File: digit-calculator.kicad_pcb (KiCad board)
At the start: 2 copper layers, 38.5 x 45 mm, 7 parts, among them J1 3V3, J2 - +, SW1 Switch, U1 XIAO this side

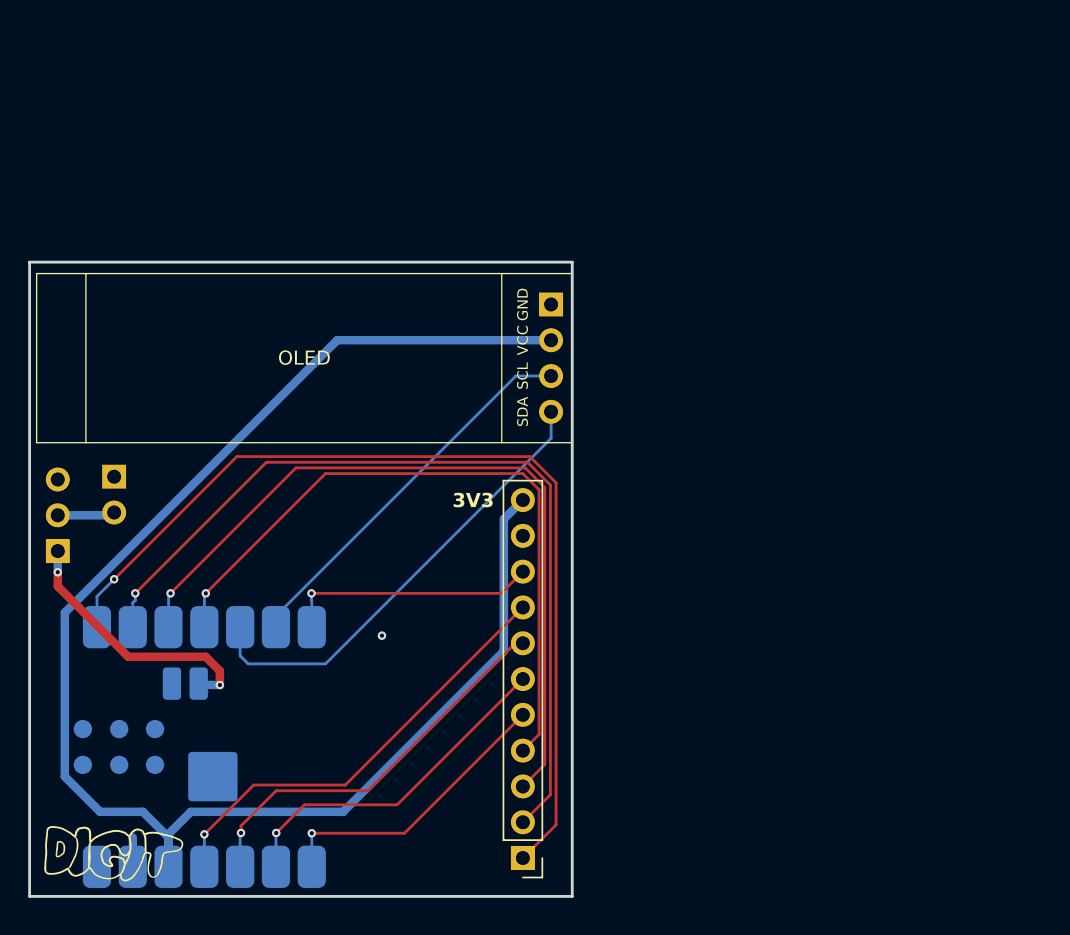
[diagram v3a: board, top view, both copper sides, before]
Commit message: switch to a bigger OLED, add more silkscreen, reroute everything, resize the board
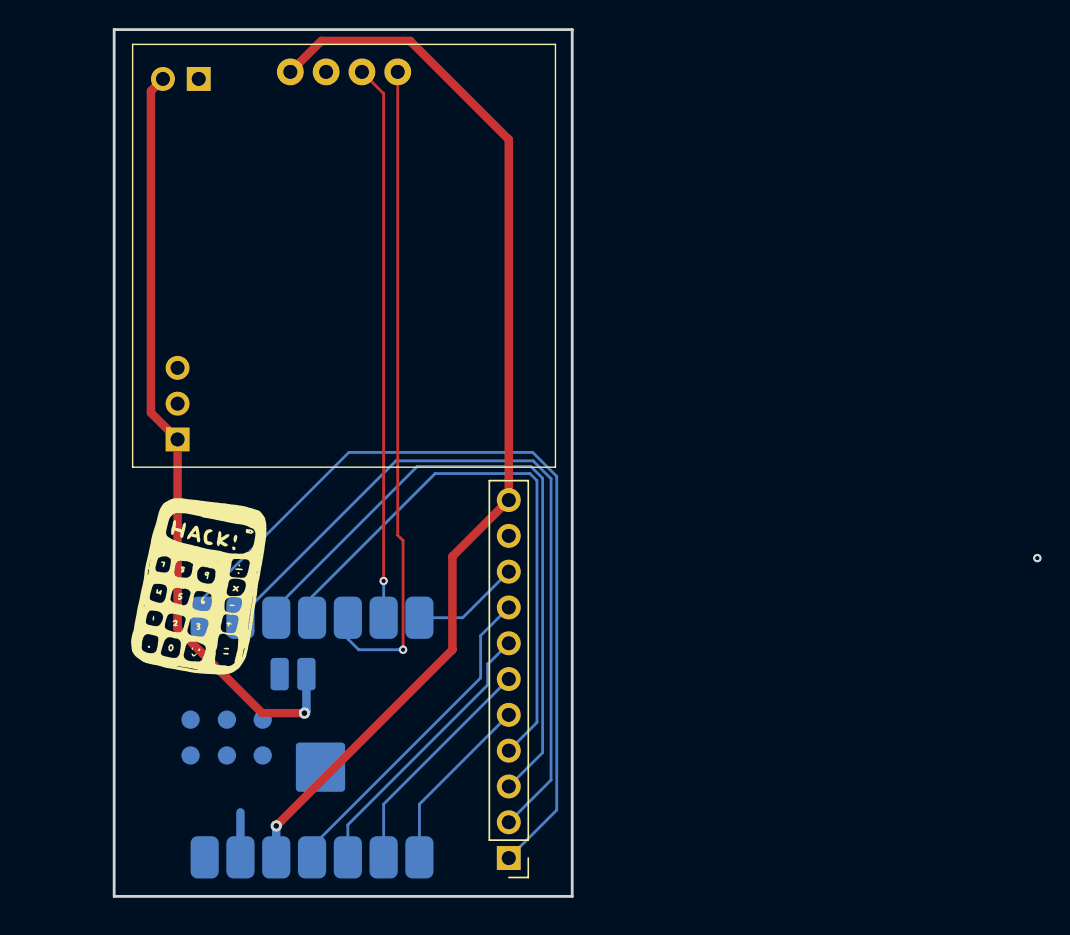
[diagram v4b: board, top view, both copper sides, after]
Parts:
- added logo: LOGO, LOGO, B.Cu at (171.0, 49.0)
- Brd1: footprint Display:SSD1306-0.91-OLED-4pin-128x32 -> Display:SSD1306-OLED
- J1: value 3V3 -> Trackball
- U1: value XIAO this side -> xiao this side down
- moved J2 28.9 mm to (156.5, 36.5), turned to 90 degrees
- moved Brd1 26.1 mm to (166.8, 36.0)
- moved G*** 19.9 mm to (156.5, 72.5)
- moved G*** 16.3 mm to (172.1, 38.7)
- moved SW1 11.6 mm to (155.0, 62.1)
- moved U1 7.67 mm to (164.5, 83.2)
- moved J1 1.00 mm to (178.5, 91.8)
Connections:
- Brd1 pad 1: GND -> +3V3
- Brd1 pad 2: +3V3 -> /SCL
- SW1 pad 2: +BATT -> Net-(SW1-B)
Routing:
- net +3V3: track 108.1 -> 77.1 mm, vias 0 -> 1
- net +BATT: track 24.0 -> 54.4 mm, vias 2 -> 1
- net /SDA: track 32.8 -> 46.9 mm, vias 0 -> 1
- net /SCL: track 27.4 -> 39.4 mm, vias 0 -> 1
- net /BTN: track 18.0 -> 7.69 mm, vias 1 -> 0
- net /J_RIGHT: track 32.9 -> 23.5 mm, vias 1 -> 0
- net /J_LEFT: track 28.3 -> 19.9 mm, vias 1 -> 0
- net /LED_R: track 61.2 -> 52.9 mm, vias 1 -> 0
- net /LED_G: track 55.1 -> 47.0 mm, vias 1 -> 0
- net /J_UP: track 20.9 -> 12.7 mm, vias 1 -> 0
- net /J_DOWN: track 24.4 -> 16.3 mm, vias 1 -> 0
- net /LED_W: track 49.1 -> 41.3 mm, vias 1 -> 0
- net /LED_B: track 67.2 -> 59.9 mm, vias 1 -> 0
- net GND: track 2.08 -> 3.19 mm, vias 1 -> 0
- net (no net): vias 0 -> 1
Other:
- board size 38.5 x 45 mm -> 32.5 x 61.5 mm
- board text added: "sda scl gnd 3v"
- board text removed: "3V3"
